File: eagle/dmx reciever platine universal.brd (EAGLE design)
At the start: 51.3 x 85.1 mm, 23 parts, among them IC1 MEGA8515-P, IC3 7805T, IC4 75176AP, Q1 6MHz

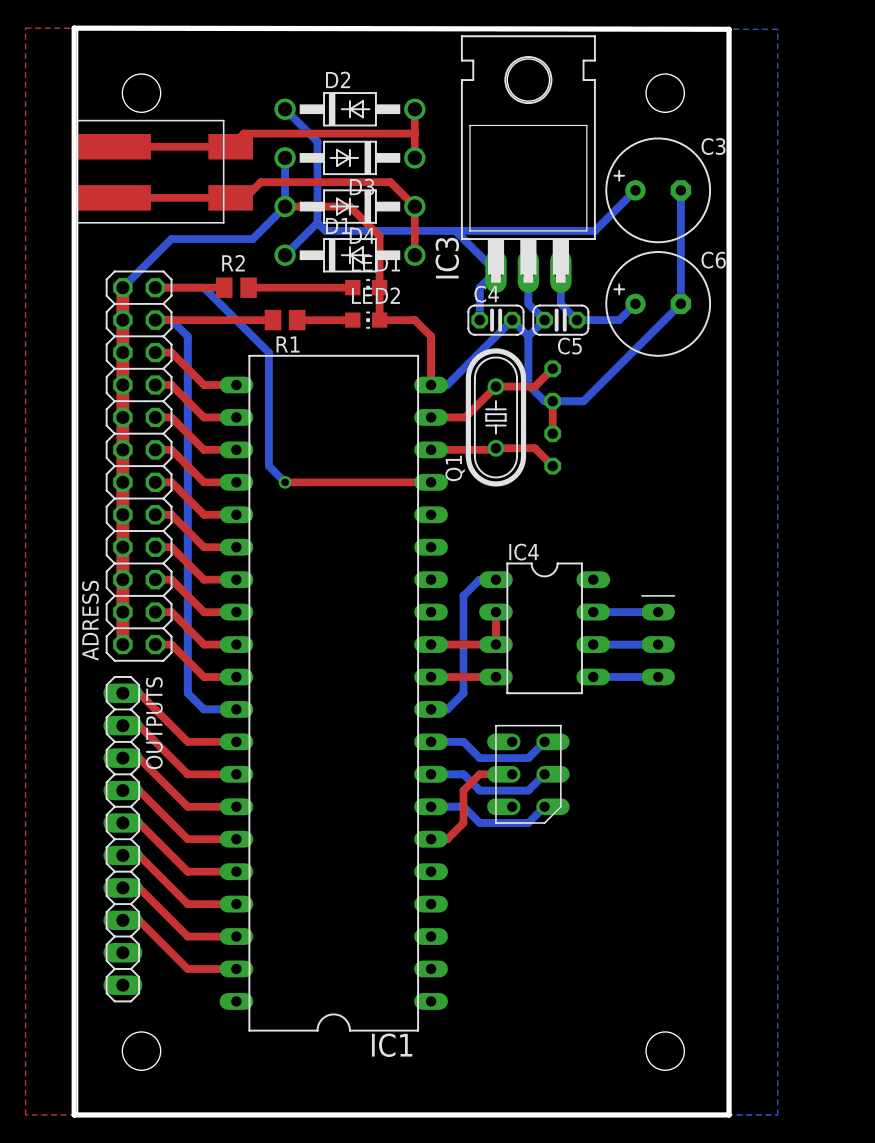
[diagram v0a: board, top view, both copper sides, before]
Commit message: new output connector
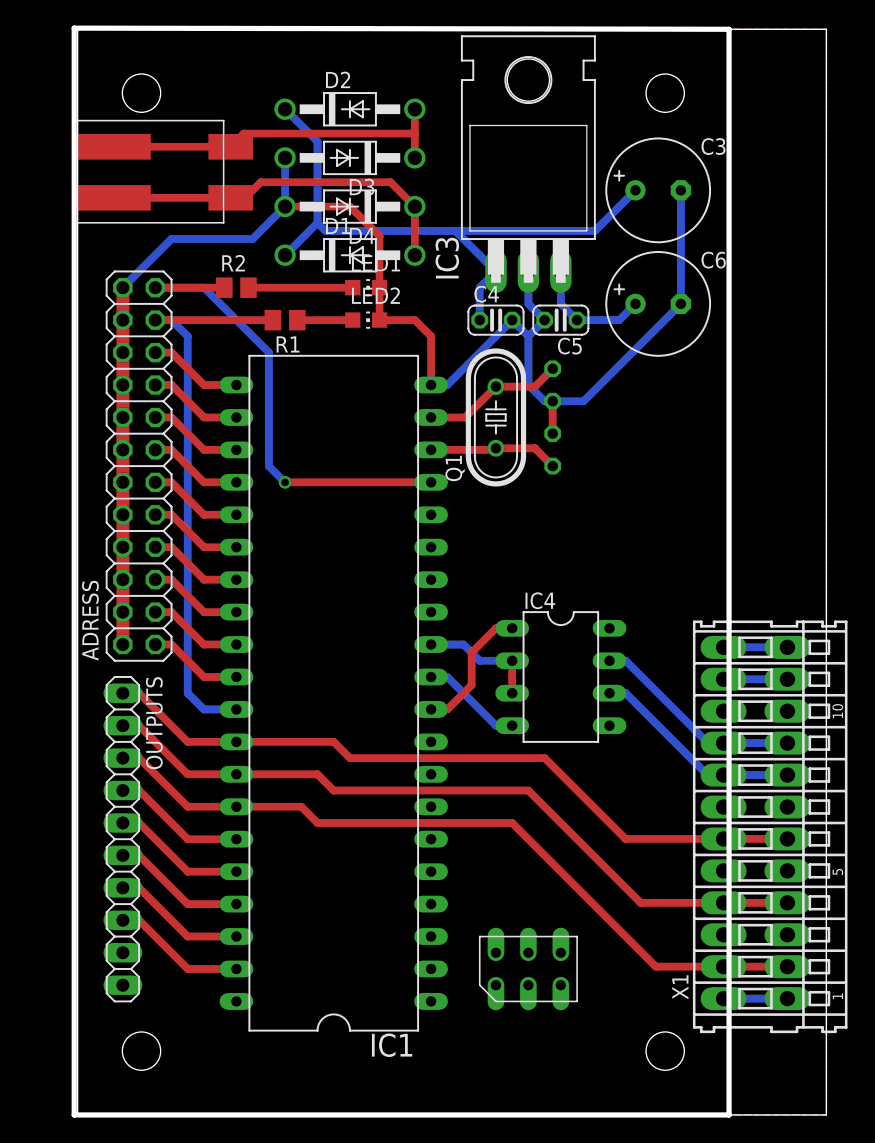
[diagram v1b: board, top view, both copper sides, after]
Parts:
- removed U$2: 1X3, stiftleisten:1X3
- added X1: (no value), con-wago:233-112
- moved ISP 15.2 mm to (34.3, 11.4), turned to 90 degrees
- moved IC4 4.02 mm to (36.8, 34.3)
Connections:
- net N$31 renamed OUTPUT4
- net N$32 renamed OUTPUT5
- net N$33 renamed OUTPUT6
- net N$34 renamed OUTPUT7
- net N$35 renamed OUTPUT8
- removed net N$13: IC4.7, U$2.P$1
- removed net N$24: IC4.6, U$2.P$2
- removed net N$28: IC1.32, OUTPUTS.1
- removed net N$29: IC1.33, OUTPUTS.2
- removed net N$30: IC1.34, OUTPUTS.3
- removed net N$36: IC4.5, U$2.P$3
- new net DMX+: IC4.6, X1.A8, X1.B8
- new net DMX-: IC4.7, X1.A9, X1.B9
- new net MOTOR+: X1.A11, X1.B11
- new net MOTOR-: X1.A12, X1.B12
- new net OUTPUT1: IC1.32, OUTPUTS.1, X1.A6, X1.B6
- new net OUTPUT2: IC1.33, OUTPUTS.2, X1.A4, X1.B4
- new net OUTPUT3: IC1.34, OUTPUTS.3, X1.A2, X1.B2
- net GND: now also IC4.5, X1.A1, X1.A10, X1.A3, X1.A5, X1.A7, X1.B1, X1.B10, X1.B3, X1.B5, X1.B7
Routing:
- net OUTPUT3: track 0.00 -> 58.8 mm
- net OUTPUT2: track 0.00 -> 57.8 mm
- net OUTPUT1: track 0.00 -> 56.8 mm
- net DMX-: track 0.00 -> 16.6 mm
- net DMX+: track 0.00 -> 16.6 mm
- net N$30: track 10.5 -> 0.00 mm
- net N$29: track 10.5 -> 0.00 mm
- net N$28: track 10.5 -> 0.00 mm
- net N$17: track 9.94 -> 0.00 mm
- net N$19: track 9.94 -> 0.00 mm
- net N$18: track 9.94 -> 0.00 mm
- net N$16: track 9.94 -> 0.00 mm
- net N$36: track 5.08 -> 0.00 mm
- net N$24: track 5.08 -> 0.00 mm
- net N$13: track 5.08 -> 0.00 mm
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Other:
- board size 51.3 x 85.1 mm -> 58.9 x 85.1 mm
